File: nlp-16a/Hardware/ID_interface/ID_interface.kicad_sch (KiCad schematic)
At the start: 0 parts

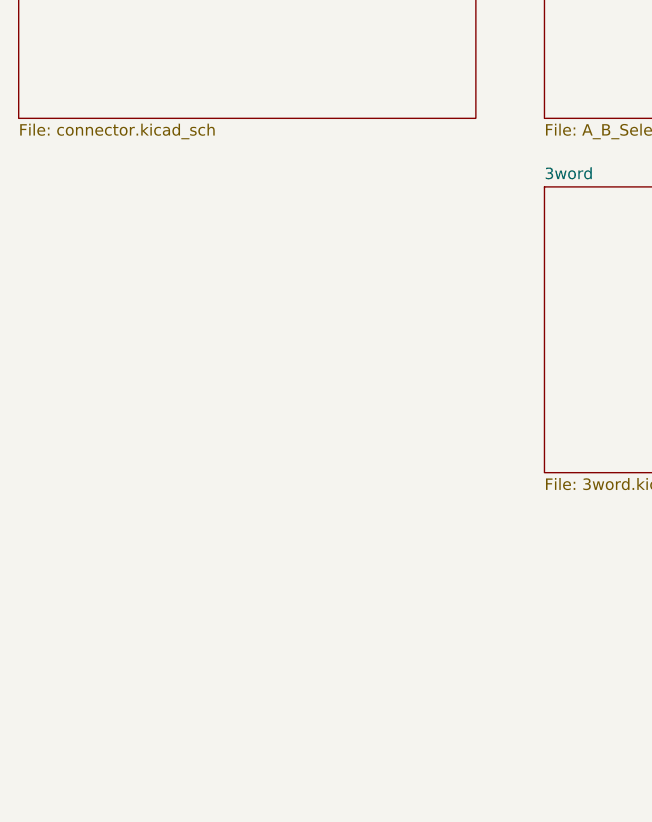
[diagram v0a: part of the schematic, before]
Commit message: 命令デコーダインターフェイスの回路がだいたいおｋ
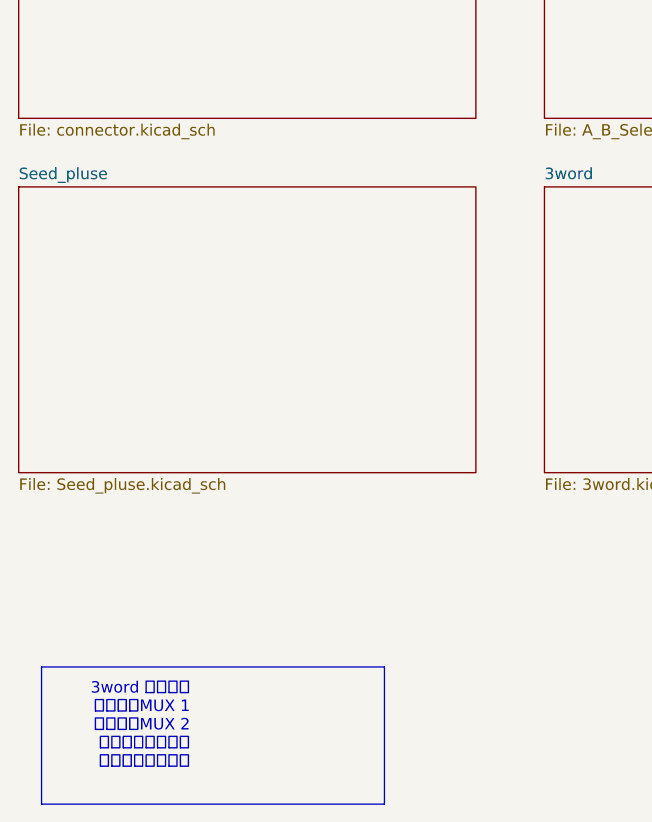
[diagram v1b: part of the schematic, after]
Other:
- added sheet Seed_pluse (Seed_pluse.kicad_sch)
- note added: "3word 命令検出 レジスタMUX 1 レジスタMUX 2 ブランチデコーダ パルスシード生成"
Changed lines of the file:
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@@
 (kicad_sch (version 20211123) (generator eeschema)
   (paper "A4")
+  (polyline (pts (xy 83.82 119.38) (xy 83.82 134.62))
+    (stroke (width 0) (type default) (color 0 0 0 0))
+  )
+  (polyline (pts (xy 45.72 119.38) (xy 83.82 119.38))
+    (stroke (width 0) (type default) (color 0 0 0 0))
+  )
+  (polyline (pts (xy 45.72 119.38) (xy 45.72 134.62))
+    (stroke (width 0) (type default) (color 0 0 0 0))
+  )
+  (polyline (pts (xy 83.82 134.62) (xy 45.72 134.62))
+    (stroke (width 0) (type default) (color 0 0 0 0))
+  )
+  (text "3word 命令検出\nレジスタMUX 1\nレジスタMUX 2\nブランチデコーダ\nパルスシード生成" (at 62.23 130.81 180)
+    (effects (font (size 1.27 1.27)) (justify right bottom))
+  )
   (text "3Unit" (at 208.28 60.96 0)
     (effects (font (size 1.27 1.27)) (justify left bottom))
@@
     )
     (property "Sheet file" "A_B_Select.kicad_sch" (id 1) (at 101.6 59.0046 0)
+      (effects (font (size 1.27 1.27)) (justify left top))
+    )
+  )
+  (sheet (at 43.18 66.04) (size 50.8 31.75) (fields_autoplaced)
+    (stroke (width 0.1524) (type solid) (color 0 0 0 0))
+    (fill (color 0 0 0 0.0000))
+    (property "Sheet name" "Seed_pluse" (id 0) (at 43.18 65.3284 0)
+      (effects (font (size 1.27 1.27)) (justify left bottom))
+    )
+    (property "Sheet file" "Seed_pluse.kicad_sch" (id 1) (at 43.18 98.3746 0)
       (effects (font (size 1.27 1.27)) (justify left top))
     )
@@
     (path "/6e5ea34e-a9ae-4bbc-bca0-35a73c8381ca" (page "5"))
     (path "/772a89e5-9ced-4a05-90e7-3a7451d9a271" (page "6"))
+    (path "/f236e9a2-3be4-4f22-a6cf-dc8d0fbb5c5a" (page "7"))
   )
   (symbol_instances
@@
       (reference "U?") (unit 1) (value "CD74HC00") (footprint "Package_DIP:DIP-14_W7.62mm")
     )
+    (path "/f236e9a2-3be4-4f22-a6cf-dc8d0fbb5c5a/4634b234-ea6a-4573-ac79-407537a347f9"
+      (reference "U?") (unit 1) (value "CD74HC00") (footprint "Package_DIP:DIP-14_W7.62mm")
+    )
     (path "/772a89e5-9ced-4a05-90e7-3a7451d9a271/46798ed5-0bbe-4ffa-bd88-fa23e0b24f59"
       (reference "U?") (unit 1) (value "CD74HC00") (footprint "Package_DIP:DIP-14_W7.62mm")
@@
       (reference "U?") (unit 1) (value "CD74HC00") (footprint "Package_DIP:DIP-14_W7.62mm")
     )
+    (path "/f236e9a2-3be4-4f22-a6cf-dc8d0fbb5c5a/4c559114-4dc9-4d40-9d48-4e0b67bd536a"
+      (reference "U?") (unit 1) (value "CD74HC00") (footprint "Package_DIP:DIP-14_W7.62mm")
+    )
     (path "/772a89e5-9ced-4a05-90e7-3a7451d9a271/4d2e99ca-a6cd-4f50-8daf-85c7425a8173"
       (reference "U?") (unit 1) (value "CD74HC00") (footprint "Package_DIP:DIP-14_W7.62mm")
@@
       (reference "U?") (unit 1) (value "CD74HC00") (footprint "Package_DIP:DIP-14_W7.62mm")
     )
+    (path "/f236e9a2-3be4-4f22-a6cf-dc8d0fbb5c5a/72a0e0b1-ecb8-4ff2-8bc1-fb75d29781e5"
+      (reference "U?") (unit 1) (value "CD74HC00") (footprint "Package_DIP:DIP-14_W7.62mm")
+    )
     (path "/6e5ea34e-a9ae-4bbc-bca0-35a73c8381ca/76e77f64-0da9-468c-8bcf-511967aec431"
       (reference "U?") (unit 1) (value "CD74HC00") (footprint "Package_DIP:DIP-14_W7.62mm")
@@
       (reference "U?") (unit 1) (value "CD74HC00") (footprint "Package_DIP:DIP-14_W7.62mm")
     )
+    (path "/f236e9a2-3be4-4f22-a6cf-dc8d0fbb5c5a/8a2ef753-bcc5-4633-96e0-9d31f0c2aa87"
+      (reference "U?") (unit 1) (value "CD74HC00") (footprint "Package_DIP:DIP-14_W7.62mm")
+    )
     (path "/6e5ea34e-a9ae-4bbc-bca0-35a73c8381ca/8f22c645-b078-4f04-81c4-5f3ba29100ba"
       (reference "U?") (unit 1) (value "CD74HC00") (footprint "Package_DIP:DIP-14_W7.62mm")
@@
       (reference "U?") (unit 1) (value "CD74HC00") (footprint "Package_DIP:DIP-14_W7.62mm")
     )
+    (path "/f236e9a2-3be4-4f22-a6cf-dc8d0fbb5c5a/b6079a62-68e3-4bca-af60-5eb9618384e7"
+      (reference "U?") (unit 1) (value "CD74HC00") (footprint "Package_DIP:DIP-14_W7.62mm")
+    )
+    (path "/f236e9a2-3be4-4f22-a6cf-dc8d0fbb5c5a/b706e94a-8858-44dc-bfec-4b5cf9c008f2"
+      (reference "U?") (unit 1) (value "CD74HC00") (footprint "Package_DIP:DIP-14_W7.62mm")
+    )
+    (path "/f236e9a2-3be4-4f22-a6cf-dc8d0fbb5c5a/bc5186e2-8195-459c-9c6a-d33251736022"
+      (reference "U?") (unit 1) (value "CD74HC00") (footprint "Package_DIP:DIP-14_W7.62mm")
+    )
     (path "/772a89e5-9ced-4a05-90e7-3a7451d9a271/bc739f60-2094-4e67-ad29-41a08060e20f"
       (reference "U?") (unit 1) (value "CD74HC00") (footprint "Package_DIP:DIP-14_W7.62mm")
@@
       (reference "U?") (unit 1) (value "CD74HC00") (footprint "Package_DIP:DIP-14_W7.62mm")
     )
+    (path "/f236e9a2-3be4-4f22-a6cf-dc8d0fbb5c5a/d83a95ed-956c-4e7a-90f7-b278b062d164"
+      (reference "U?") (unit 1) (value "CD74HC00") (footprint "Package_DIP:DIP-14_W7.62mm")
+    )
     (path "/6e5ea34e-a9ae-4bbc-bca0-35a73c8381ca/d89be282-d8f0-49fa-9e7d-ec287c094949"
       (reference "U?") (unit 1) (value "CD74HC00") (footprint "Package_DIP:DIP-14_W7.62mm")
     )
+    (path "/f236e9a2-3be4-4f22-a6cf-dc8d0fbb5c5a/d8b97530-bbd6-424d-bfd1-01f30be4a231"
+      (reference "U?") (unit 1) (value "CD74HC00") (footprint "Package_DIP:DIP-14_W7.62mm")
+    )
     (path "/772a89e5-9ced-4a05-90e7-3a7451d9a271/d94a521f-8fe8-49e8-beea-99985ea77666"
       (reference "U?") (unit 1) (value "CD74HC00") (footprint "Package_DIP:DIP-14_W7.62mm")
     )
+    (path "/f236e9a2-3be4-4f22-a6cf-dc8d0fbb5c5a/de9422c6-1cf6-44dc-87a8-7dc73fff3bad"
+      (reference "U?") (unit 1) (value "CD74HC00") (footprint "Package_DIP:DIP-14_W7.62mm")
+    )
     (path "/772a89e5-9ced-4a05-90e7-3a7451d9a271/def69910-5a27-44aa-a588-241c65f586be"
       (reference "U?") (unit 1) (value "CD74HC00") (footprint "Package_DIP:DIP-14_W7.62mm")
@@
       (reference "U?") (unit 1) (value "CD74HC00") (footprint "Package_DIP:DIP-14_W7.62mm")
     )
+    (path "/f236e9a2-3be4-4f22-a6cf-dc8d0fbb5c5a/f34ae421-2366-4b75-9d23-39f0d296f112"
+      (reference "U?") (unit 1) (value "CD74HC00") (footprint "Package_DIP:DIP-14_W7.62mm")
+    )

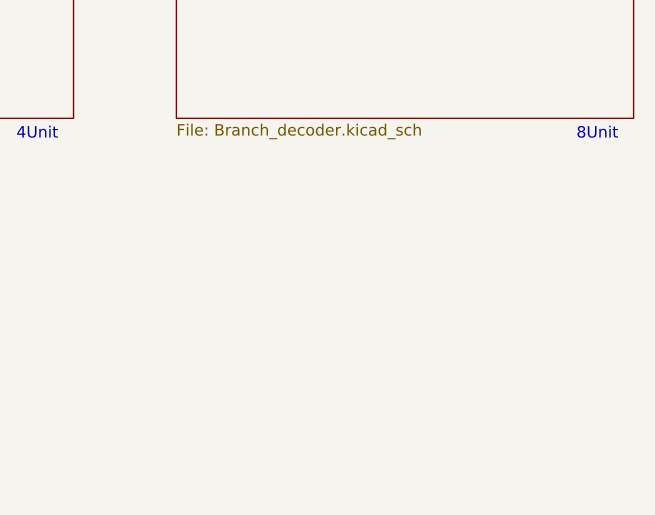
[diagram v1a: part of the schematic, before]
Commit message: 命令デコーダとの配線方法を変更
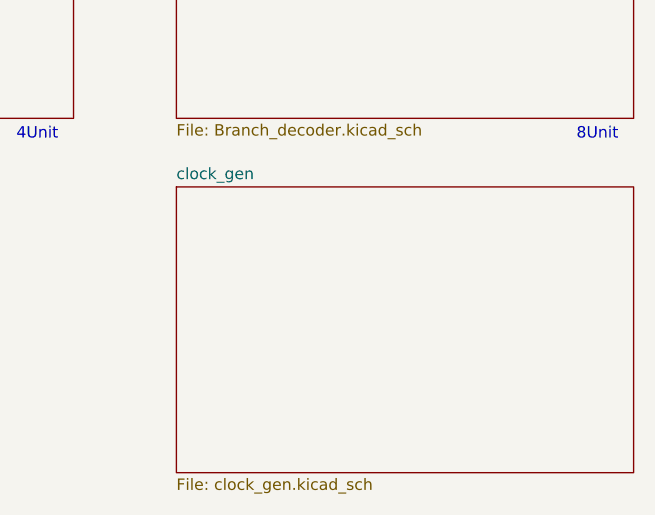
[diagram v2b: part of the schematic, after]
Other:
- added sheet clock_gen (clock_gen.kicad_sch)
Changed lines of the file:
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@@
+    )
+  )
+  (sheet (at 163.83 105.41) (size 50.8 31.75) (fields_autoplaced)
+    (stroke (width 0.1524) (type solid) (color 0 0 0 0))
+    (fill (color 0 0 0 0.0000))
+    (property "Sheet name" "clock_gen" (id 0) (at 163.83 104.6984 0)
+      (effects (font (size 1.27 1.27)) (justify left bottom))
+    )
+    (property "Sheet file" "clock_gen.kicad_sch" (id 1) (at 163.83 137.7446 0)
+      (effects (font (size 1.27 1.27)) (justify left top))
     )
   )
@@
     (path "/772a89e5-9ced-4a05-90e7-3a7451d9a271" (page "6"))
     (path "/f236e9a2-3be4-4f22-a6cf-dc8d0fbb5c5a" (page "7"))
+    (path "/064cadae-a90a-403a-8102-4e246e642879" (page "8"))
   )
   (symbol_instances
-    (path "/f318d57b-e1ce-4958-abcf-445d253cb285/3c547ea3-6bb9-4f09-bdea-2b8fea5cedca"
+    (path "/f236e9a2-3be4-4f22-a6cf-dc8d0fbb5c5a/46c14653-1460-40d9-b772-067ab357ee57"
       (reference "#PWR?") (unit 1) (value "GND") (footprint "")
     )
     (path "/6e5ea34e-a9ae-4bbc-bca0-35a73c8381ca/5e8d6cd9-e566-40b9-98ad-cd350b0e5223"
-      (reference "#PWR?") (unit 1) (value "GND") (footprint "")
-    )
-    (path "/f318d57b-e1ce-4958-abcf-445d253cb285/a0379853-d09a-42dd-bfec-a42da161770e"
       (reference "#PWR?") (unit 1) (value "GND") (footprint "")
     )
@@
       (reference "#PWR?") (unit 1) (value "GND") (footprint "")
     )
-    (path "/f318d57b-e1ce-4958-abcf-445d253cb285/05ae1262-467e-4f00-bd7e-137853c58a91"
-      (reference "J?") (unit 1) (value "Conn_02x10_Counter_Clockwise") (footprint "Connector_PinHeader_2.54mm:PinHeader_2x10_P2.54mm_Horizontal")
+    (path "/f318d57b-e1ce-4958-abcf-445d253cb285/1d7aadf7-2cff-4de0-9295-1e2dc4effd89"
+      (reference "J?") (unit 1) (value "Conn_02x10_Odd_Even") (footprint "Connector_PinHeader_2.54mm:PinHeader_2x10_P2.54mm_Horizontal")
     )
-    (path "/f318d57b-e1ce-4958-abcf-445d253cb285/89b2a68e-97b8-4f69-9240-089980ce0b77"
+    (path "/f318d57b-e1ce-4958-abcf-445d253cb285/705b8f01-8923-4f03-81b8-ba9dbc5b94cb"
       (reference "J?") (unit 1) (value "Conn_02x10_Odd_Even") (footprint "Connector_PinHeader_2.54mm:PinHeader_2x10_P2.54mm_Horizontal")
     )
     (path "/f318d57b-e1ce-4958-abcf-445d253cb285/a6ea1d00-8748-4fc0-a095-d6475427330d"
       (reference "J?") (unit 1) (value "Conn_02x10_Counter_Clockwise") (footprint "Connector_PinHeader_2.54mm:PinHeader_2x10_P2.54mm_Horizontal")
-    )
-    (path "/f318d57b-e1ce-4958-abcf-445d253cb285/be1722b4-886a-4765-b773-b19c52ac9f09"
-      (reference "J?") (unit 1) (value "Conn_02x10_Odd_Even") (footprint "Connector_PinHeader_2.54mm:PinHeader_2x10_P2.54mm_Horizontal")
     )
     (path "/f318d57b-e1ce-4958-abcf-445d253cb285/bfb68bc3-cd5e-4ad2-99a8-66300bc83f74"
@@
     (path "/f318d57b-e1ce-4958-abcf-445d253cb285/de60a7f5-5432-4835-9ded-2ffdac2badc0"
       (reference "J?") (unit 1) (value "Conn_02x10_Odd_Even") (footprint "Connector_PinHeader_2.54mm:PinHeader_2x10_P2.54mm_Horizontal")
-    )
-    (path "/f318d57b-e1ce-4958-abcf-445d253cb285/f1cc3e39-b62e-4601-bae0-337eedc48e6f"
-      (reference "J?") (unit 1) (value "Conn_02x10_Counter_Clockwise") (footprint "Connector_PinHeader_2.54mm:PinHeader_2x10_P2.54mm_Horizontal")
     )
     (path "/6e5ea34e-a9ae-4bbc-bca0-35a73c8381ca/01423451-804e-4bd7-a610-2a3a3b327dda"
@@
       (reference "U?") (unit 1) (value "CD74HC00") (footprint "Package_DIP:DIP-14_W7.62mm")
     )
+    (path "/f236e9a2-3be4-4f22-a6cf-dc8d0fbb5c5a/3639b663-c8a0-400f-8af5-6f25ad038e04"
+      (reference "U?") (unit 1) (value "CD74HC00") (footprint "Package_DIP:DIP-14_W7.62mm")
+    )

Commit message: 命令デコーダインターフェイスだいたい完了！！
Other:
- removed sheet A_B_Select
- removed sheet A_Y_Select
- removed sheet clock_gen
- added sheet BUS_selector (BUS_selector.kicad_sch)
- added sheet INT_ACQ (INT_ACQ.kicad_sch)
- note added: "3word 命令検出 レジスタMUX(統合) ・レジスタMUX 1 ・レジスタMUX 2 ブランチデコーダ パルスシード生成"
- note removed: "3word 命令検出 レジスタMUX 1 レジスタMUX 2 ブランチデコーダ パルスシード生成"
